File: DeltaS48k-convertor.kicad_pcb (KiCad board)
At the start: 2 copper layers, 97 x 48.7 mm, 3 parts, among them J1 SNP, J2 ZX1

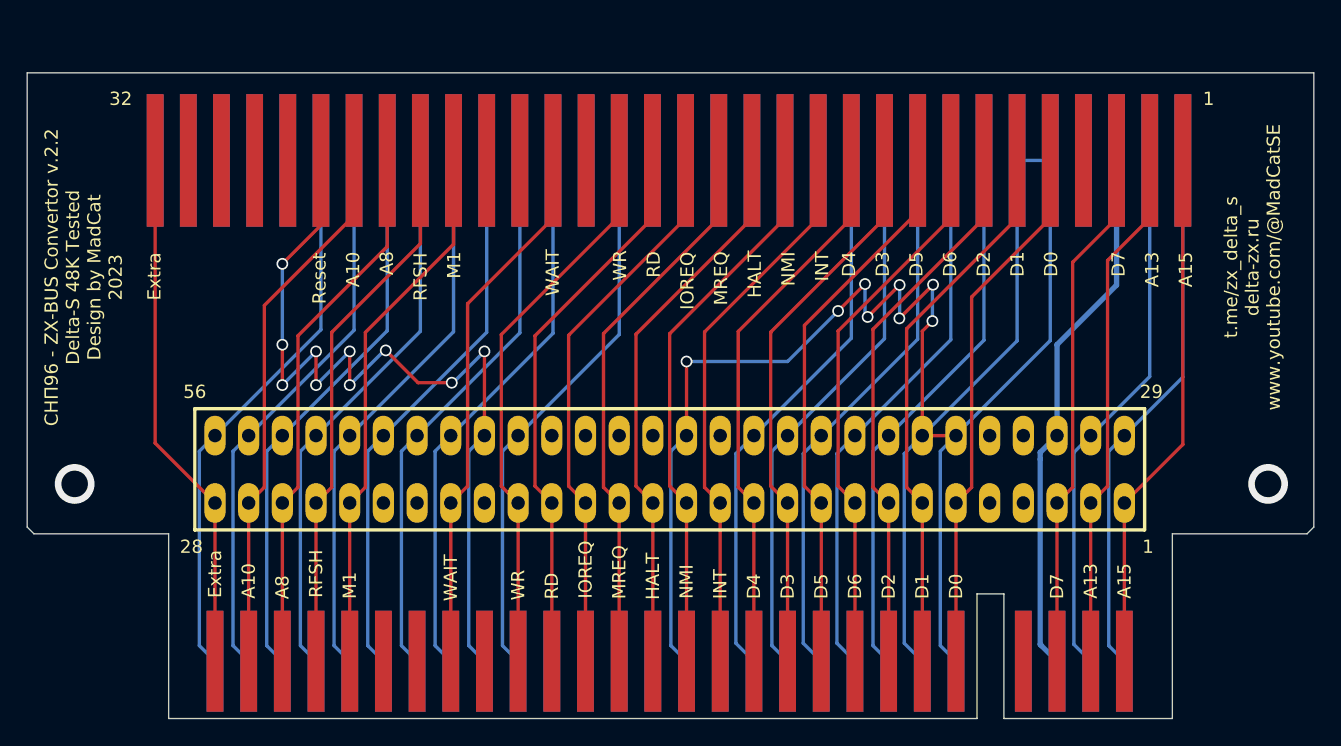
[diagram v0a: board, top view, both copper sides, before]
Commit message: Fixed ZX Bus conector width
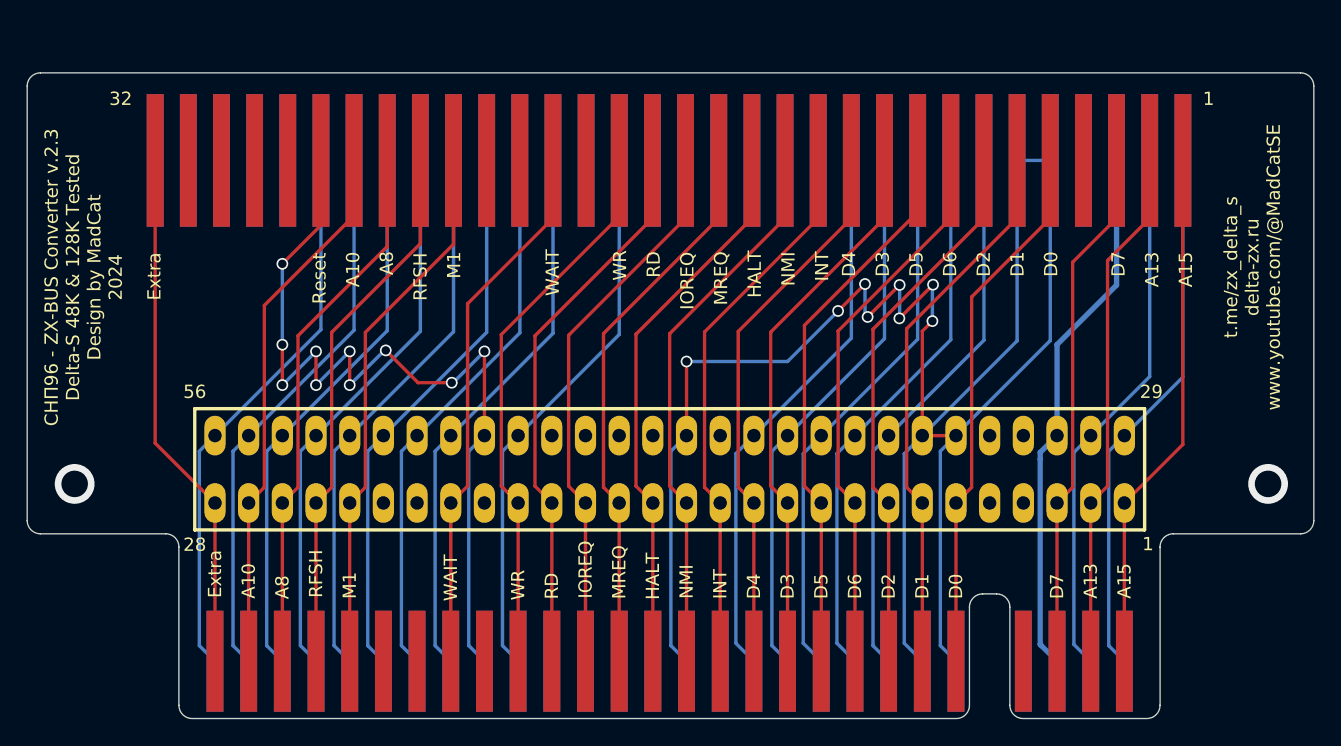
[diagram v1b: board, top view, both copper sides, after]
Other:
- outline, holes or cut-outs redrawn
- board text added: "СНП96 - ZX-BUS Converter v.2.3 Delta-S 48K & 128K Tested Design by MadCat 2024"
- board text removed: "СНП96 - ZX-BUS Convertor v.2.2 Delta-S 48K Tested Design by MadCat 2023"
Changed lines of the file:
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@@
       (net 72 "A11") (pinfunction "A11") (pintype "input"))
   )
-  (gr_line (start 175.44802 35.00202) (end 78.42002 35.00202)
-    (stroke (width 0.1) (type solid)) (layer "Edge.Cuts"))
-  (gr_line (start 78.42002 35.00202) (end 78.42002 69.25351)
-    (stroke (width 0.1) (type solid)) (layer "Edge.Cuts"))
-  (gr_line (start 78.42002 69.25351) (end 78.92802 69.76151)
-    (stroke (width 0.1) (type solid)) (layer "Edge.Cuts"))
-  (gr_line (start 152.08002 83.693) (end 164.78002 83.693)
-    (stroke (width 0.1) (type solid)) (layer "Edge.Cuts"))
-  (gr_line (start 78.92802 69.76151) (end 89.08802 69.76151)
-    (stroke (width 0.1) (type solid)) (layer "Edge.Cuts"))
-  (gr_line (start 150.04802 83.693) (end 150.04802 74.295)
-    (stroke (width 0.1) (type solid)) (layer "Edge.Cuts"))
-  (gr_line (start 152.08002 74.295) (end 152.08002 83.693)
-    (stroke (width 0.1) (type solid)) (layer "Edge.Cuts"))
-  (gr_line (start 164.78002 69.76151) (end 174.94002 69.76151)
-    (stroke (width 0.1) (type solid)) (layer "Edge.Cuts"))
-  (gr_line (start 175.44802 69.25351) (end 175.44802 35.00202)
-    (stroke (width 0.1) (type solid)) (layer "Edge.Cuts"))
-  (gr_line (start 89.08802 83.693) (end 150.04802 83.693)
-    (stroke (width 0.1) (type solid)) (layer "Edge.Cuts"))
-  (gr_line (start 174.94002 69.76151) (end 175.44802 69.25351)
-    (stroke (width 0.1) (type solid)) (layer "Edge.Cuts"))
-  (gr_line (start 150.04802 74.295) (end 152.08002 74.295)
-    (stroke (width 0.1) (type solid)) (layer "Edge.Cuts"))
-  (gr_line (start 164.78002 83.693) (end 164.78002 69.76151)
-    (stroke (width 0.1) (type solid)) (layer "Edge.Cuts"))
-  (gr_line (start 89.08802 69.76151) (end 89.08802 83.693)
-    (stroke (width 0.1) (type solid)) (layer "Edge.Cuts"))
+  (gr_arc (start 175.44802 68.76151) (mid 175.155127 69.468617) (end 174.44802 69.76151)
+    (stroke (width 0.1) (type default)) (layer "Edge.Cuts"))
+  (gr_arc (start 79.42002 69.76151) (mid 78.712913 69.468617) (end 78.42002 68.76151)
+    (stroke (width 0.1) (type default)) (layer "Edge.Cuts"))
+  (gr_line (start 174.44802 35.00202) (end 79.42002 35.00202)
+    (stroke (width 0.1) (type solid)) (layer "Edge.Cuts"))
+  (gr_line (start 78.42002 36.00202) (end 78.42002 68.76151)
+    (stroke (width 0.1) (type solid)) (layer "Edge.Cuts"))
+  (gr_line (start 163.851 82.693) (end 163.851 70.76151)
+    (stroke (width 0.1) (type default)) (layer "Edge.Cuts"))
+  (gr_line (start 153.527 83.693) (end 162.851 83.693)
+    (stroke (width 0.1) (type solid)) (layer "Edge.Cuts"))
+  (gr_arc (start 151.527 74.295) (mid 152.234107 74.587893) (end 152.527 75.295)
+    (stroke (width 0.1) (type default)) (layer "Edge.Cuts"))
+  (gr_arc (start 90.863 83.693) (mid 90.155893 83.400107) (end 89.863 82.693)
+    (stroke (width 0.1) (type default)) (layer "Edge.Cuts"))
+  (gr_line (start 89.863 82.693) (end 89.863 70.76151)
+    (stroke (width 0.1) (type default)) (layer "Edge.Cuts"))
+  (gr_arc (start 149.479 82.693) (mid 149.186107 83.400107) (end 148.479 83.693)
+    (stroke (width 0.1) (type default)) (layer "Edge.Cuts"))
+  (gr_line (start 79.42002 69.76151) (end 88.863 69.76151)
+    (stroke (width 0.1) (type solid)) (layer "Edge.Cuts"))
+  (gr_line (start 149.479 82.693) (end 149.479 75.295)
+    (stroke (width 0.1) (type solid)) (layer "Edge.Cuts"))
+  (gr_line (start 152.527 75.295) (end 152.527 82.693)
+    (stroke (width 0.1) (type solid)) (layer "Edge.Cuts"))
+  (gr_arc (start 78.42002 36.00202) (mid 78.712907 35.294907) (end 79.42002 35.00202)
+    (stroke (width 0.1) (type default)) (layer "Edge.Cuts"))
+  (gr_line (start 164.851 69.76151) (end 174.44802 69.76151)
+    (stroke (width 0.1) (type solid)) (layer "Edge.Cuts"))
+  (gr_line (start 175.44802 68.76151) (end 175.44802 36.00202)
+    (stroke (width 0.1) (type solid)) (layer "Edge.Cuts"))
+  (gr_arc (start 153.527 83.693) (mid 152.819893 83.400107) (end 152.527 82.693)
+    (stroke (width 0.1) (type default)) (layer "Edge.Cuts"))
+  (gr_arc (start 163.851 82.693) (mid 163.558107 83.400107) (end 162.851 83.693)
+    (stroke (width 0.1) (type default)) (layer "Edge.Cuts"))
+  (gr_line (start 90.863 83.693) (end 148.479 83.693)
+    (stroke (width 0.1) (type solid)) (layer "Edge.Cuts"))
+  (gr_arc (start 88.863 69.76151) (mid 89.570103 70.054404) (end 89.863 70.76151)
+    (stroke (width 0.1) (type default)) (layer "Edge.Cuts"))
+  (gr_arc (start 163.851 70.76151) (mid 164.14389 70.054397) (end 164.851 69.76151)
+    (stroke (width 0.1) (type default)) (layer "Edge.Cuts"))
+  (gr_arc (start 149.479 75.295) (mid 149.771893 74.587893) (end 150.479 74.295)
+    (stroke (width 0.1) (type default)) (layer "Edge.Cuts"))
+  (gr_line (start 150.479 74.295) (end 151.527 74.295)
+    (stroke (width 0.1) (type solid)) (layer "Edge.Cuts"))
+  (gr_arc (start 174.44802 35.00202) (mid 175.155107 35.294922) (end 175.44802 36.00202)
+    (stroke (width 0.1) (type default)) (layer "Edge.Cuts"))
   (gr_text "A9" (at 95.123 74.437666 90) (layer "B.SilkS")
     (effects (font (size 1 1) (thickness 0.15)) (justify mirror))
@@
     (effects (font (size 1 1) (thickness 0.15)))
   )
-  (gr_text "28" (at 90.805 70.739) (layer "F.SilkS")
+  (gr_text "28" (at 91.059 70.5866) (layer "F.SilkS")
     (effects (font (size 1 1) (thickness 0.15)))
   )
@@
     (effects (font (size 1 1) (thickness 0.15)))
   )
-  (gr_text "СНП96 - ZX-BUS Convertor v.2.2\nDelta-S 48K Tested\nDesign by MadCat\n2023" (at 82.677 50.419 90) (layer "F.SilkS")
+  (gr_text "СНП96 - ZX-BUS Converter v.2.3\nDelta-S 48K & 128K Tested\nDesign by MadCat\n2024" (at 82.677 50.419 90) (layer "F.SilkS")
     (effects (font (size 1 1) (thickness 0.15)))
   )
@@
     (effects (font (size 1 1) (thickness 0.15)))
   )
-  (gr_text "1" (at 162.941 70.739) (layer "F.SilkS")
-    (effects (font (size 1 1) (thickness 0.15)))
-  )
+  (gr_text "1" (at 162.941 70.5358) (layer "F.SilkS")
+    (effects (font (size 1 1) (thickness 0.15)))
+  )
